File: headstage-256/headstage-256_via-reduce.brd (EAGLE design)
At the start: 32 x 32 mm, 302 parts, among them J2 MMCX-J-P-H-ST-SM1/U.FL-R-SMT(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, J4 PINHD-2X5+4DF40-HEAD, J5 5041940270, U1 OPA170, U10 NRF24L01QFN, U11 CAT4016_QFN, U12 CAT4016_QFN, U13 TPL0501_UQFN, U14 TPL0501_UQFN, U15 MICROSD_473093751, U16 10M08SAM15317G, U17 Si8487DB, U18 MAX17048_WLP, U19 BNO055, U2 OPA170, U20 TPS61202, U21 RHD2064_BGA, U22 RHD2064_BGA, U23 TS4231, U24 TS4231, U25 LT3463, U26 ASCO-50.000MHZ-EK-T3, U27 TS4231, U28 TLV70733, U29 TS4231, U3 INA826, U30 RHD2064_BGA, U31 RHD2064_BGA, U32 MIC23150, U33 TS4231, U34 TS4231, U35 TPS8268180, U4 INA826, U5 DAC5311, U6 DAC5311, U7 DS90UB913A_WQFN, U8 DG509B, U9 DG509B, Y1 FW1600008, Y2 ECS-.327-12.5-1210-TR

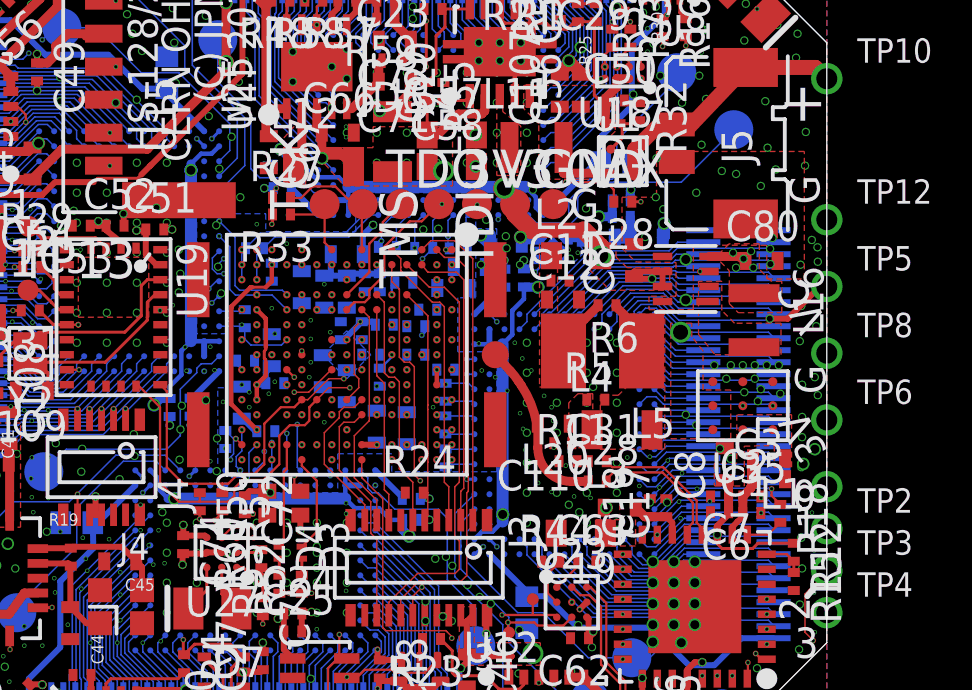
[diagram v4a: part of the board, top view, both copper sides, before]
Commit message: Even more catious routing on headstage-256
- Serializer digital lines completely avoid bias-t network's inductor
and pads.
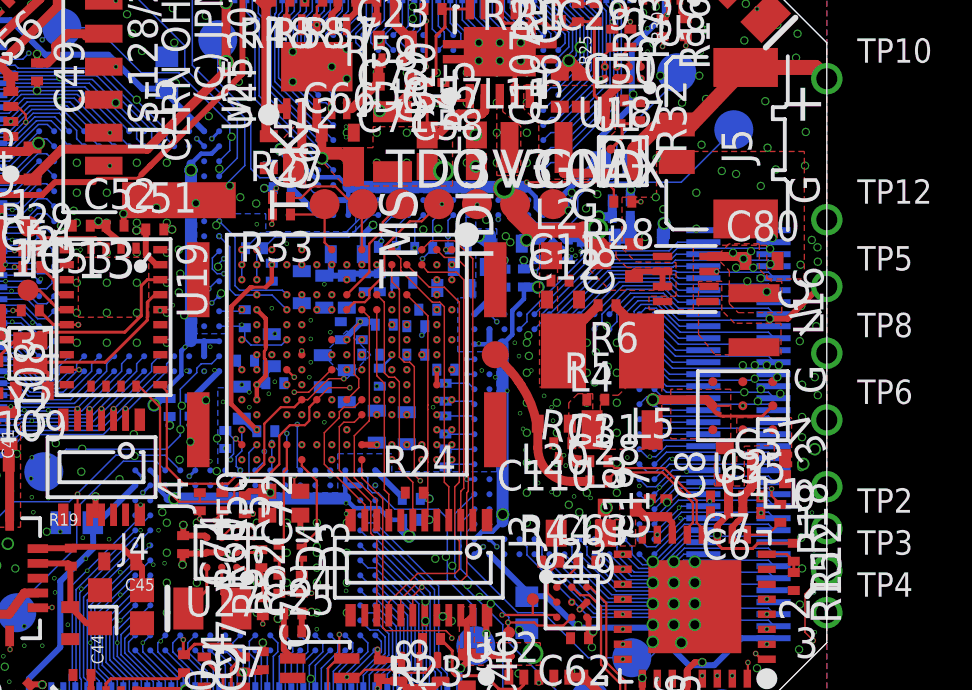
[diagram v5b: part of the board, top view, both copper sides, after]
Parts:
- moved R11 0.05 mm to (7.37, -3.90), turned to 352 degrees
- moved C28 0.05 mm to (8.40, -4.62)
- moved C31 0.05 mm to (8.40, -3.95)
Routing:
- net VCOAX: track 70.4 -> 77.9 mm, vias 16 -> 12
- net HSYNC: track 18.4 -> 21.7 mm
- net DIN8: track 18.2 -> 21.5 mm
- net DIN9: track 17.9 -> 21.2 mm
- net DIN10: track 19.3 -> 22.5 mm
- net SERDES_EN: track 14.8 -> 17.9 mm
- net DIN11: track 19.5 -> 22.6 mm
- net SERDES_SDA: track 17.9 -> 20.8 mm
- net SERDES_SCL: track 18.5 -> 21.4 mm
- net PCLK: track 22.0 -> 24.8 mm
- net VSYNC: track 20.0 -> 22.8 mm
- net GND: track 40.4 -> 39.5 mm, vias 451 -> 455
- net LIPO_QSTRT: track 10.9 -> 10.2 mm
- net !LIPO_ALRT: track 14.3 -> 13.7 mm
- net +3V3: vias 50 -> 53

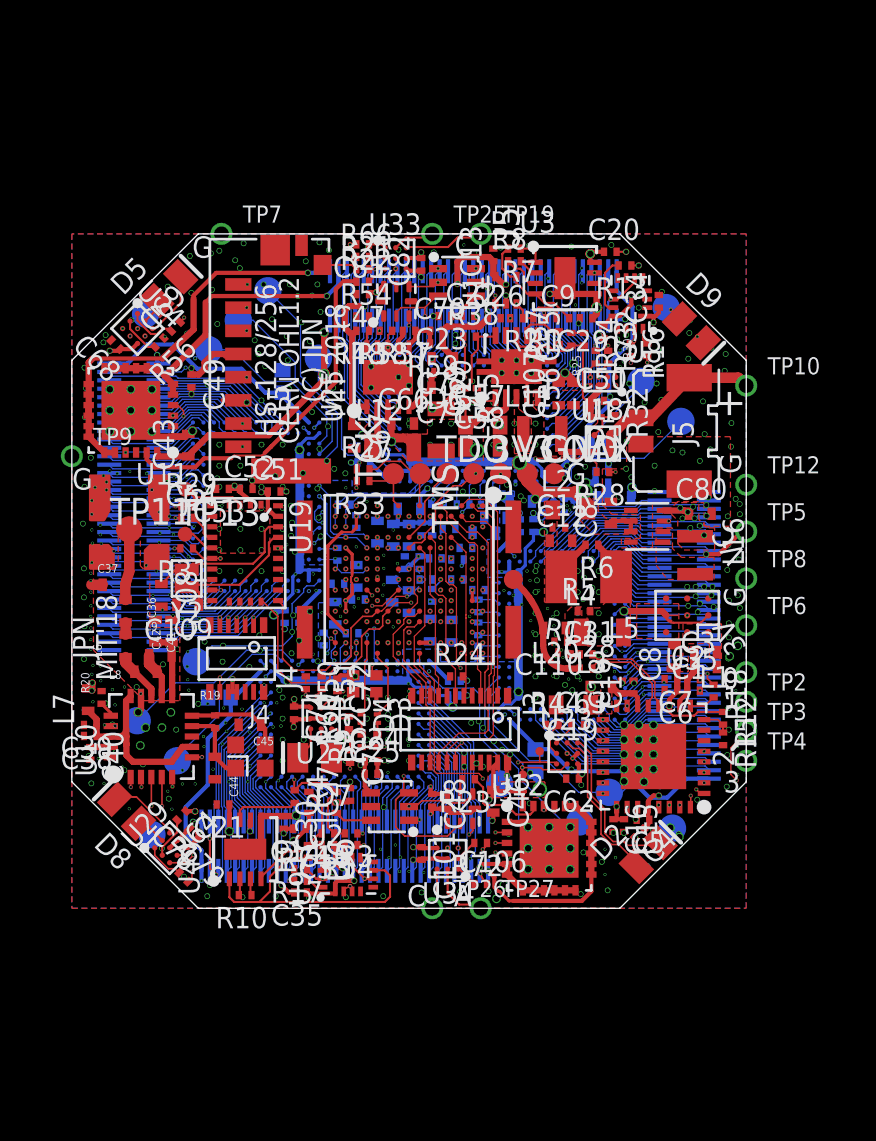
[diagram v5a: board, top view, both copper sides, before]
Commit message: Produced gerbers for headstage-256 rev. 1.1
- Should be ready for production
- Updated schematic
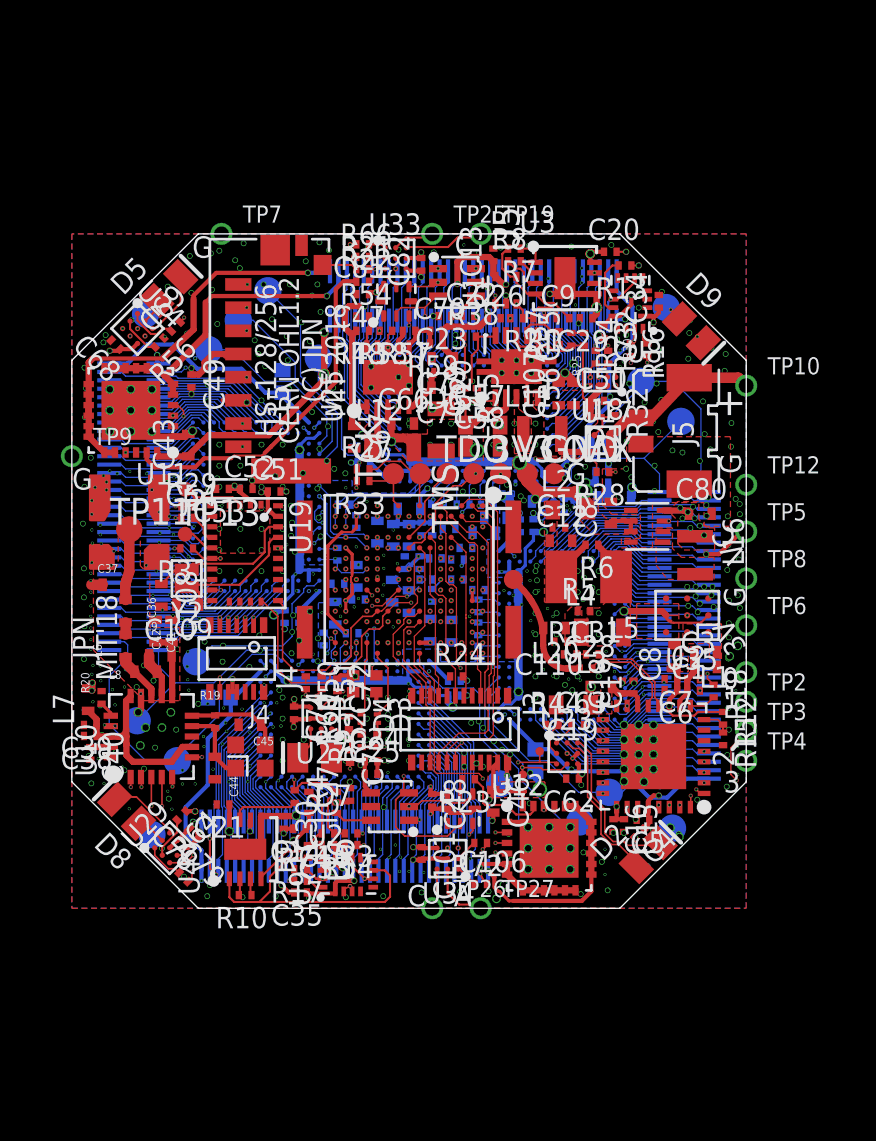
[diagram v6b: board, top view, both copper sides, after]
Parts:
- moved C31 0.30 mm to (8.70, -3.95)
- moved R11 0.29 mm to (7.65, -3.95), turned to 0 degrees
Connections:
- net AUXIN1_A: now also JD.34
- net AUXIN1_B: now also JC.34
- net AUXIN2_A: now also JD.36
- net AUXIN2_B: now also JC.36
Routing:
- net AUXIN1_B: track 8.05 -> 17.1 mm
- net AUXIN1_A: track 8.27 -> 17.1 mm
- net AUXIN2_A: track 9.24 -> 11.1 mm
- net AUXIN2_B: track 8.95 -> 10.8 mm
- net AGND: vias 273 -> 275

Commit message: Some final changes to headstage-256
- Replace UFL wirelss coax connector with IPEX connector
- Ground plane improvements
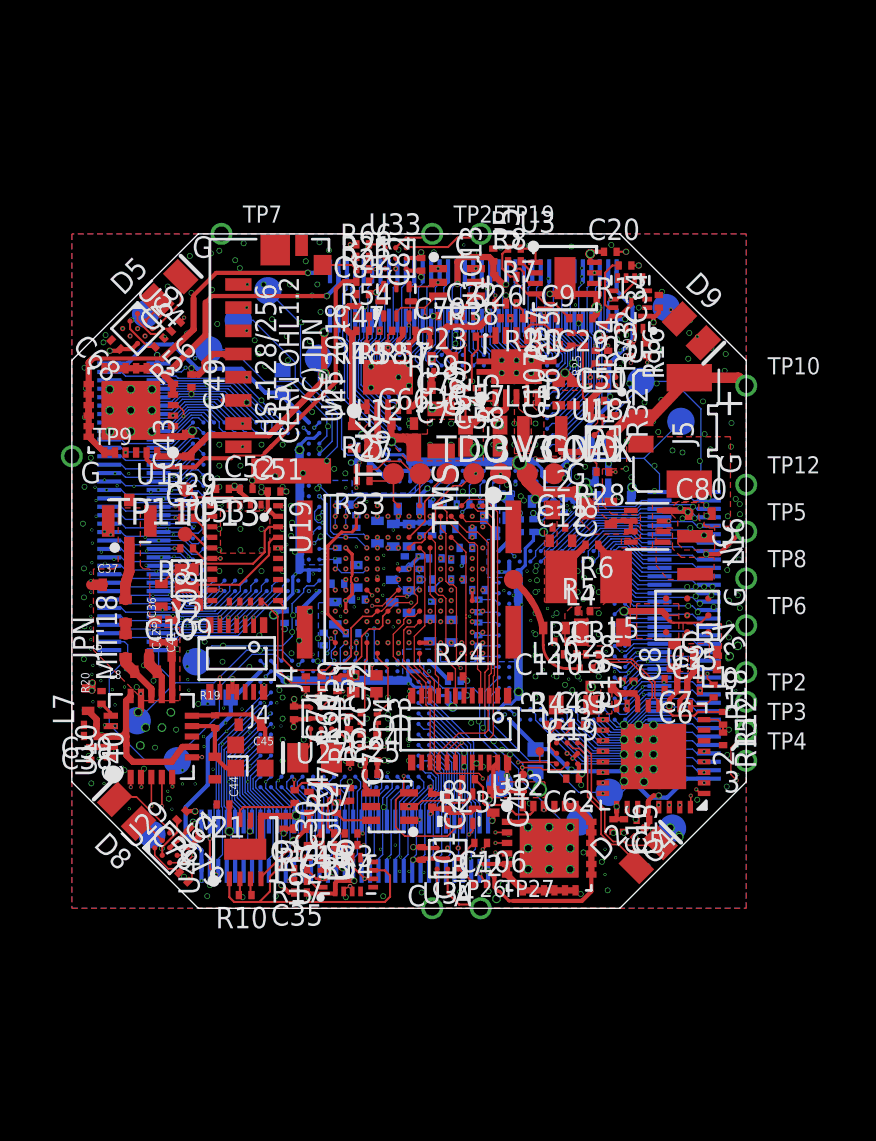
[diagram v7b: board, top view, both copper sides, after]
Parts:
- J2: device jonnew:MMCX/U.FL -> jonnew:X_FL_R_SMT_1(02)
- moved J2 1.10 mm to (-13.3, 2.38)
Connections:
- net ANT: now also J2.P$1; no longer J2.SIG1
- net GND: now also J2.P$2, J2.P$3, J2.P$4; no longer J2.GND@1, J2.GND@2, J2.GND@3, J2.GND@4
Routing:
- net ANT: track 3.37 -> 2.67 mm
- net GND: vias 455 -> 457
- added copper zone on layer 2, net N$39
- added copper zone on layer 4, net N$39
- added copper zone on layer 5, net N$39
- added copper zone on layer 2, net N$44
- added copper zone on layer 4, net N$44
- added copper zone on layer 5, net N$44
- added copper zone on layer 2, net N$45
- added copper zone on layer 4, net N$45
- added copper zone on layer 5, net N$45
- added copper zone on layer 2, net N$69
- added copper zone on layer 4, net N$69
- removed copper zone on layer 3, net N$69

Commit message: Headstage-256 rev. 1.1
- Ready for speedy
- Moved the coax adapter boards to tabbed daughter boards on the
headstage-256 PCB
- Lots of small fixes during final DRC and gerber creation
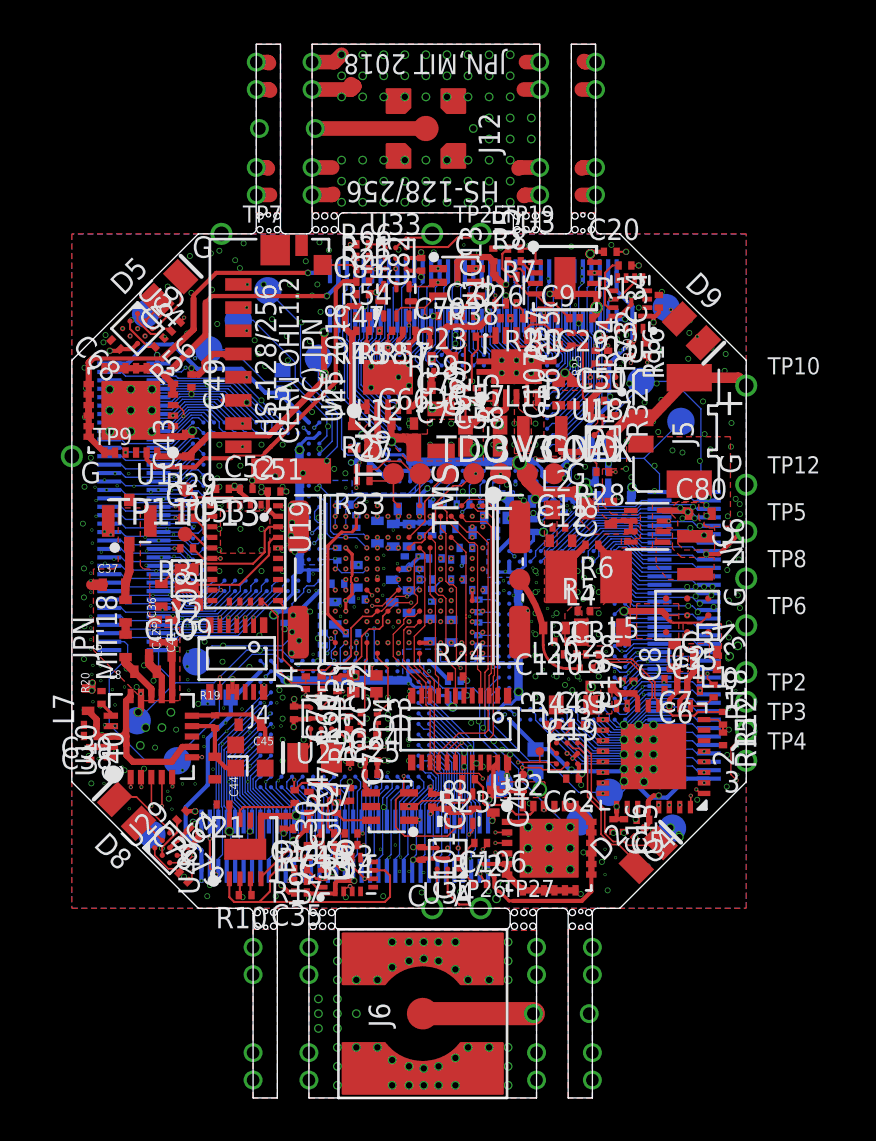
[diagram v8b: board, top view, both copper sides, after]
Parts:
- added J11, J17: (no value), jonnew:COAX-ADAPTER-8X8MM-GND-THRU
- added J12: MMCX-J-P-H-ST-SM1, jonnew:MMCX-SMT-VERT
- added J13, J7: (no value), jonnew:COAX-ADAPTER-8X8MM-THRU
- added J15, J9: (no value), jonnew:COAX-ADAPTER-8X8MM-SIG-THRU
- added J6: 142-0711-201, jonnew:SMA_VERT
- JA, JB, JC, JD: value (none) -> DF40C(2.0)-70DS-0.4V(51)
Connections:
- new net ADAPT_SIG: J12.SIG, J13.SIG, J15.SIG, J6.SIG, J7.SIG, J9.SIG
- new net GND1: J11.GND1, J11.GND2, J11.GND3, J11.GND4, J12.GND@1, J12.GND@2, J12.GND@3, J12.GND@4, J13.GND1, J13.GND12, J13.GND2, J13.GND3, J13.GND5, J13.GND6, J13.GND7, J13.GND9, J15.GND1, J15.GND2, J15.GND3, J15.GND4, J17.GND1, J17.GND2, J17.GND3, J17.GND4, J6.G1, J6.G2, J6.G3, J6.G4, J7.GND1, J7.GND12, J7.GND2, J7.GND3, J7.GND5, J7.GND6, J7.GND7, J7.GND9, J9.GND1, J9.GND2, J9.GND3, J9.GND4
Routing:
- net GND1: track 0.00 -> 14.0 mm, vias 0 -> 108
- net ADAPT_SIG: track 0.00 -> 10.5 mm
- net GND: vias 457 -> 459
- added copper zone on layer 1, net GND1
- added copper zone on layer 16, net GND1
- removed copper zone on layer 4, net N$39
- removed copper zone on layer 5, net N$39
- removed copper zone on layer 4, net N$44
- removed copper zone on layer 5, net N$44
- removed copper zone on layer 4, net N$45
- removed copper zone on layer 5, net N$45
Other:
- board size 32 x 32 mm -> 32 x 50 mm
- board text added: "JPN,MIT 2018"
